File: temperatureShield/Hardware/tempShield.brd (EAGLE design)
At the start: 57.1 x 31.8 mm, 33 parts, among them U1 SHT30, U2 TMP007, U3 FUJITSU_MB85RS1MT

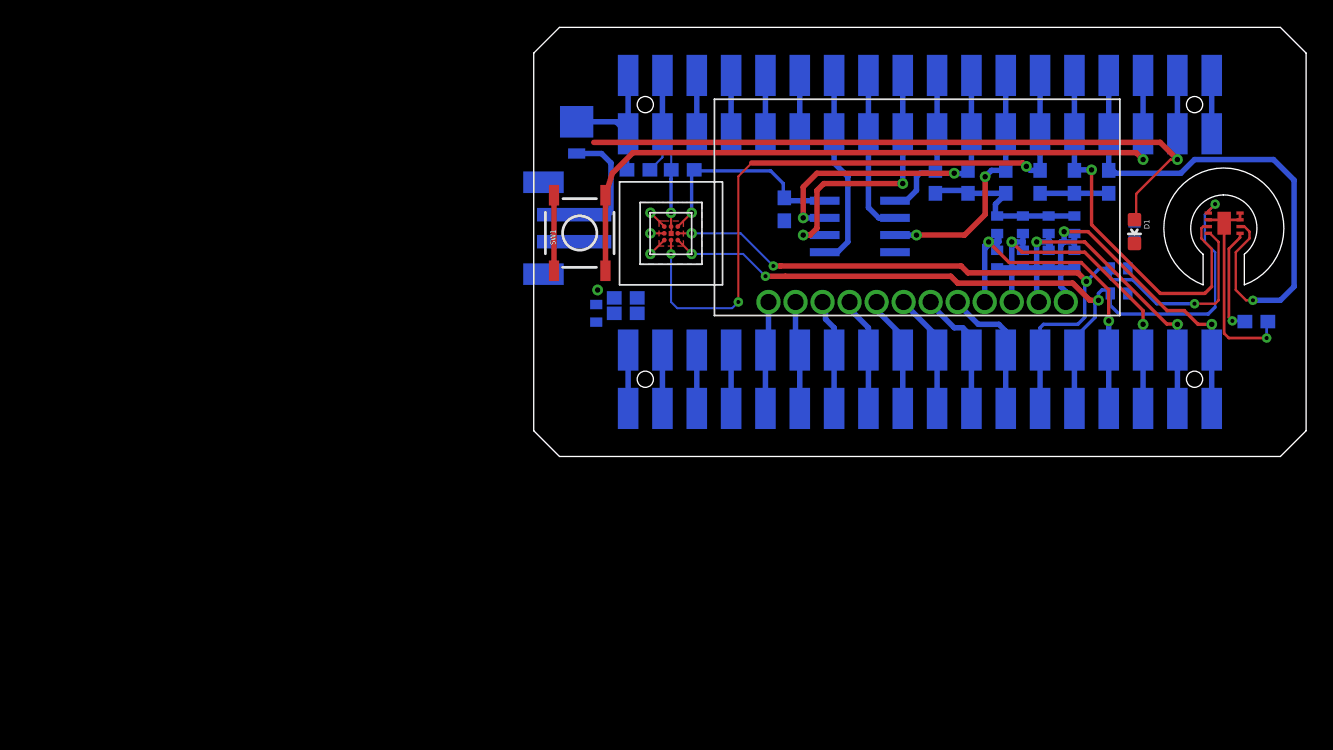
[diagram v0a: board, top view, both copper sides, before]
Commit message: almost finish the layout,the package of diode need to be double check
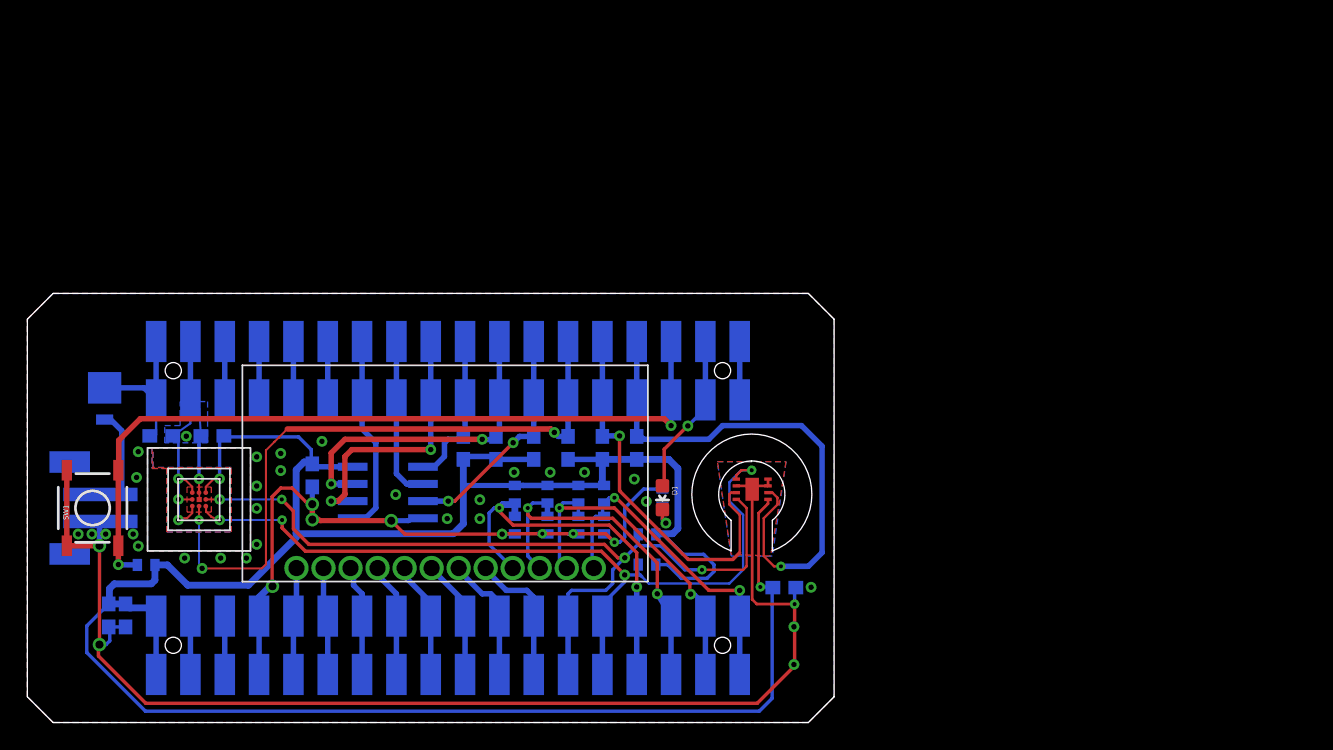
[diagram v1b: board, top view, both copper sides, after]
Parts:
- moved C4 44.3 mm to (6.02, 7.92), turned to 90 degrees
- moved C5 43.8 mm to (7.26, 7.92), turned to 90 degrees
- moved SW1 41.4 mm to (4.83, 15.9)
- moved R7 40.9 mm to (36.1, 16.9)
- moved R12 40.8 mm to (36.1, 14.6)
- moved JP1 40.7 mm to (3.40, 15.9)
- moved R8 40.4 mm to (38.5, 16.9)
- moved C6 40.4 mm to (9.91, 21.2)
- moved R13 40.3 mm to (38.5, 14.6)
- moved R18 40.3 mm to (45.8, 11.7)
- moved R10 40.1 mm to (42.7, 16.9)
- moved R9 40.1 mm to (40.8, 16.9)
- moved U$4 40.1 mm to (31.1, 15.9)
- moved C2 40.1 mm to (56.0, 9.98)
- moved D1 40.1 mm to (47.0, 16.6)
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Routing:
- net +3V3: track 48.0 -> 185.6 mm
- net GND: track 51.5 -> 179.8 mm, vias 5 -> 45
- net N$2: track 56.0 -> 13.8 mm
- net N$4: track 53.6 -> 58.6 mm
- net COM1: track 28.6 -> 25.2 mm
- net N$5: track 0.00 -> 2.47 mm, vias 0 -> 1
- net !WP: track 18.8 -> 17.2 mm
- net COM3: track 26.0 -> 27.5 mm
- net N$3: track 9.23 -> 7.75 mm
- net COM4: track 27.4 -> 28.6 mm
- net SCL: track 61.6 -> 62.8 mm
- net SDA: track 61.8 -> 62.8 mm
- net !ALERT: track 49.2 -> 48.3 mm
- added copper zone on layer 1, net N$14
- added copper zone on layer 16, net N$15
- added copper zone on layer 16, net N$16
- added copper zone on layer 1, net N$17
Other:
- board size 57.1 x 31.8 mm -> 59.7 x 31.8 mm
